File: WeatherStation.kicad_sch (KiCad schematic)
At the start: 9 parts

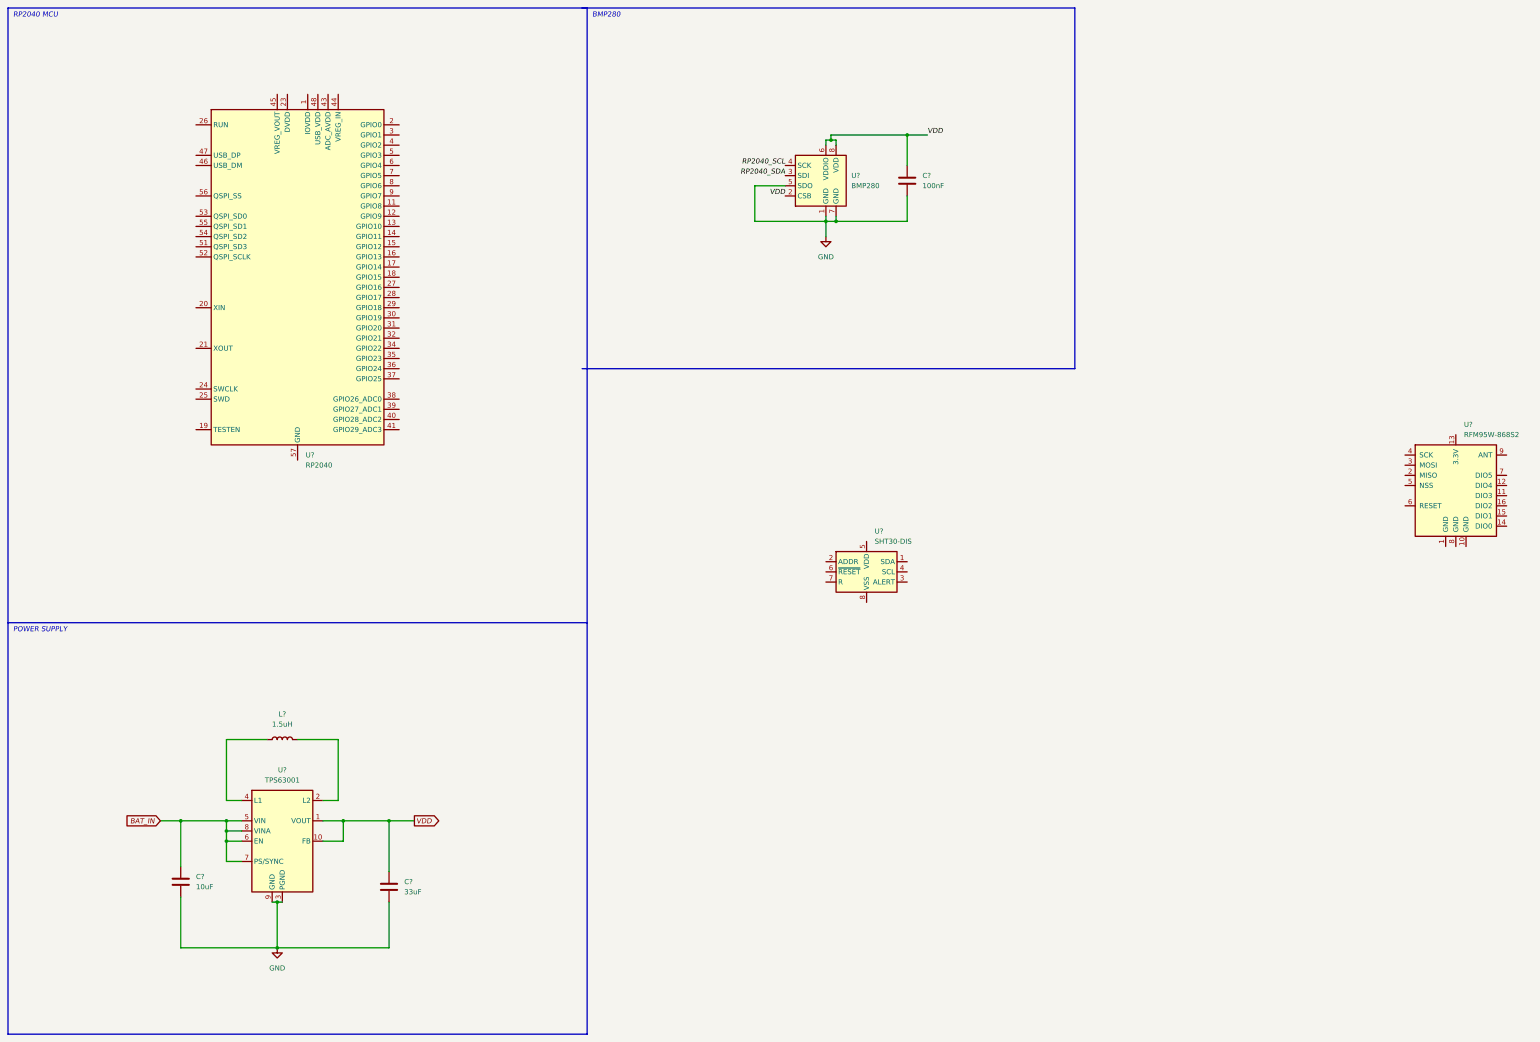
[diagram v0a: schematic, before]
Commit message: some capatitiors and sensors
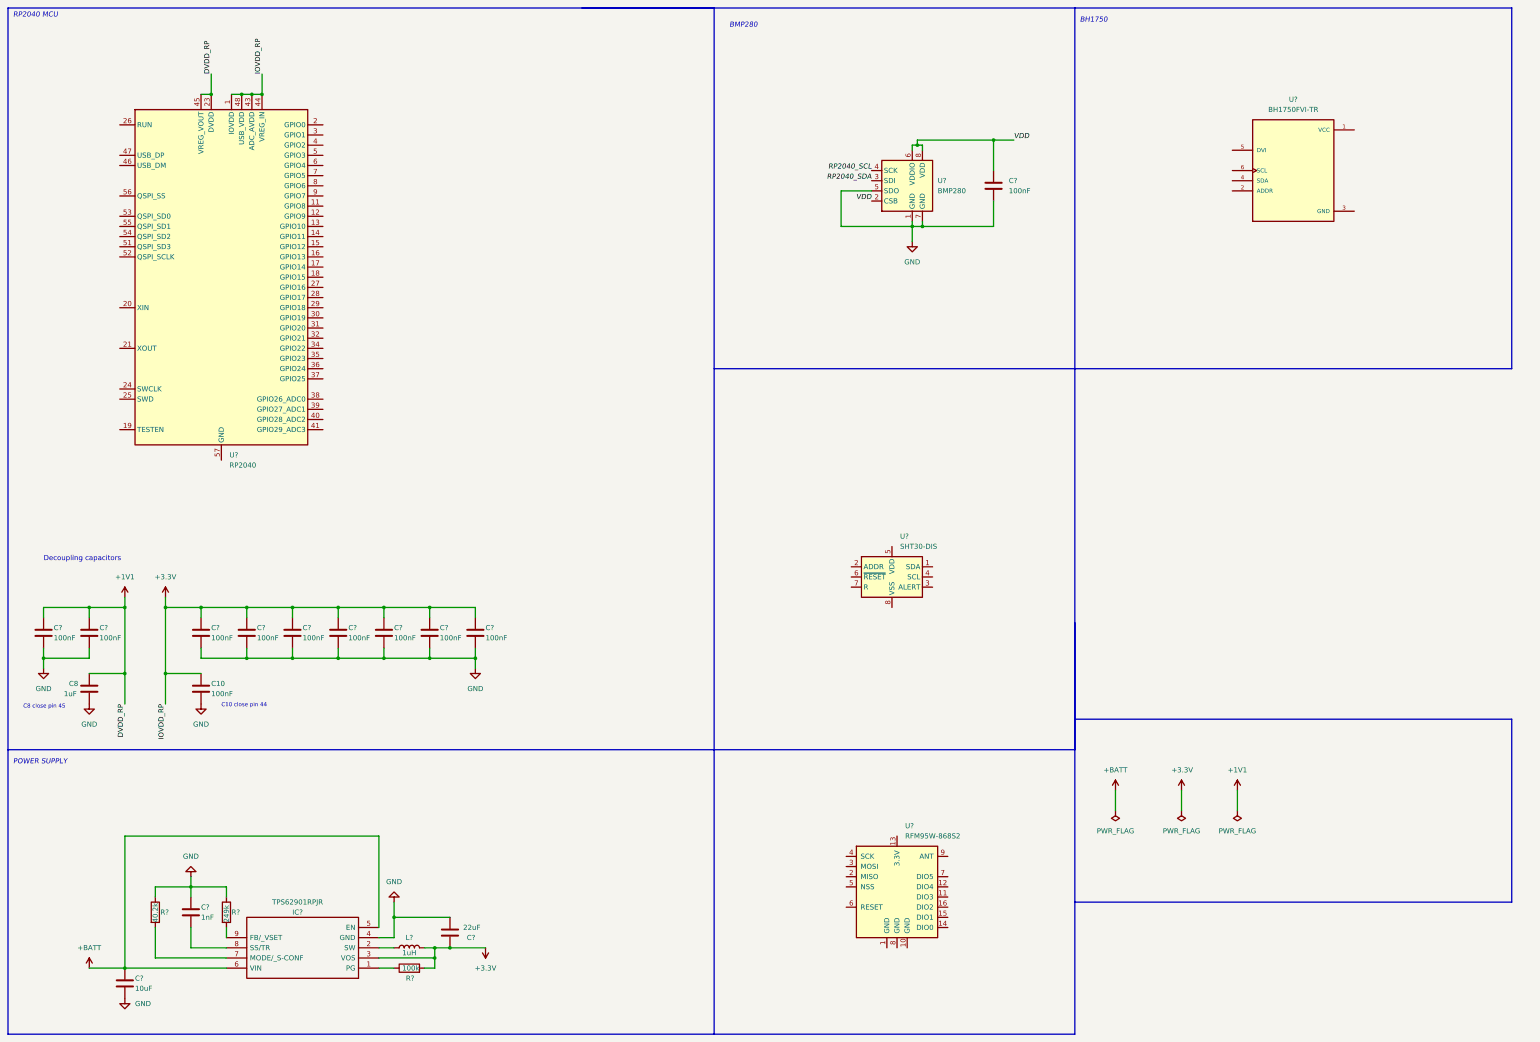
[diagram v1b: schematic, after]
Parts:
- removed C?: 33uF, symbol Device:C
- removed C?: 10uF, symbol Device:C
- removed L?: 1.5uH, symbol Device:L
- removed U?: TPS63001, Package_SON:Texas_DRC0010J_ThermalVias, symbol Regulator_Switching:TPS63001
- added C10, C? (x9): 100nF, symbol Device:C
- added C8: 1uF, symbol Device:C
- added C?: 22uF, symbol Device:C
- added C?: 1nF, symbol Device:C
- added C?: 10uF, symbol Device:C
- added IC?: TPS62901RPJR, TPS62901RPJR, symbol TPS62901RPJR:TPS62901RPJR
- added L?: 1uH, symbol Device:L
- added R?: 40.2k, symbol Device:R
- added R?: 249k, symbol Device:R
- added R?: 100k, symbol Device:R
- added U?: BH1750FVI-TR, XDCR_BH1750FVI-TR, symbol BH1750:BH1750FVI-TR
- U?: footprint (none) -> RF_Module:HOPERF_RFM9XW_SMD
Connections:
- net GND: now also C10.2, C8.2, C?.1, C?.2, C?.2, C?.2, C?.2, C?.2, C?.2, C?.2, C?.2, C?.2, C?.2, C?.2, IC?.4 (GND), R?.1, R?.1
- net +3.3V: now reaches U?.1 (IOVDD), U?.10 (IOVDD), U?.22 (IOVDD), U?.33 (IOVDD), U?.42 (IOVDD), U?.49 (IOVDD)
- net +3.3V: now also U?.43 (ADC_AVDD), U?.44 (VREG_IN), U?.48 (USB_VDD), C10.1, C?.1, C?.1, C?.1, C?.1, C?.1, C?.1, C?.1, C?.1, IC?.3 (VOS), L?.2, R?.2
- net +1V1: now reaches U?.23 (DVDD), U?.50 (DVDD)
- net +1V1: now also U?.45 (VREG_VOUT), C8.1, C?.1, C?.1
- new net: IC?.7 (MODE/_S-CONF), R?.2
- new net: IC?.1 (PG), R?.1
- new net: IC?.2 (SW), L?.1
- new net: C?.2, IC?.8 (SS/TR)
- new net: IC?.9 (FB/_VSET), R?.2
- new net +BATT: C?.1, IC?.5 (EN), IC?.6 (VIN)
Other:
- note added: "BH1750"
- note added: "C10 close pin 44"
- note added: "C8 close pin 45"
- note added: "Decoupling capacitors"
- moved on the sheet: C?, U?

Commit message: kabelki
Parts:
- added AE?: Antenna, symbol Device:Antenna
- added C? (x2): 27pF, symbol Device:C
- added C?: 0.1uF, symbol Device:C
- added C? (x2): 100nF, symbol Device:C
- added C?: 10uF, symbol Device:C_Polarized
- added J? (x2): Conn_01x02, symbol Connector_Generic:Conn_01x02
- added R? (x4): 1k, symbol Device:R
- added R? (x4): 10k, symbol Device:R
- added R? (x2): 27, symbol Device:R
- added R?: DNF, symbol Device:R
- added U?: W25Q128JVSIQ, SOIC127P790X216-8N, symbol Flashs:W25Q128JVSIQ
- added Y?: Crystal, symbol Device:Crystal
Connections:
- net VDD is gone; now on net +3.3V: C?.1, U?.2 (CSB), U?.6 (VDDIO), U?.8 (VDD)
- net +3.3V: now also U?.1 (VCC), U?.5 (VDD), C?.1, C?.1, C?.2, R?.1, R?.1, R?.1, R?.2, R?.2, R?.2, U?.8 (VCC)
- net GND: now also U?.1 (GND), U?.10 (GND), U?.2 (ADDR), U?.3 (GND), U?.57 (GND), U?.6 (RESET), U?.6 (~{RESET}), U?.7 (R), U?.8 (GND), U?.8 (VSS), U?.9 (VSS), C?.1, C?.1, C?.1, C?.2, C?.2, C?.2, J?.2 (Pin_2), R?.1, U?.4 (GND)
- net at U?.2 (ADDR): now also R?.2
- net SDA: now reaches U?.4 (SDA)
- net SDA: now also U?.1 (SDA), R?.1, R?.2
- net at U?.5 (DVI): now also C?.1, R?.1
- net SCL: now reaches U?.6 (SCL)
- net SCL: now also U?.4 (SCL), R?.1, R?.2
- net GPIO_ALERT_SHT30: now reaches U?.3 (ALERT)
- net GPIO_ALERT_SHT30: now also U?.2 (GPIO0)
- net DIO2_LORA: now reaches U?.11 (DIO3)
- net DIO1_LORA: now reaches U?.12 (DIO4)
- net DIO5_LORA: now reaches U?.14 (DIO0)
- net DIO4_LORA: now reaches U?.15 (DIO1)
- net DIO3_LORA: now reaches U?.16 (DIO2)
- net MISO_LORA: now reaches U?.2 (MISO)
- net MOSI_LORA: now reaches U?.3 (MOSI)
- net SCK_LORA: now reaches U?.4 (SCK)
- net CS_LORA: now reaches U?.5 (NSS)
- net DIO0_LORA: now reaches U?.7 (DIO5)
- net at U?.9 (ANT): now also AE?.1 (A)
- net TESTEN: now reaches U?.19 (TESTEN)
- net XIN: now reaches U?.20 (XIN)
- net XIN: now also C?.2, Y?.2
- net XOUT: now reaches U?.21 (XOUT)
- net XOUT: now also R?.2
- net SWCLK: now reaches U?.24 (SWCLK)
- net SWD: now reaches U?.25 (SWD)
- net RUN: now reaches U?.26 (RUN)
- net at U?.46 (USB_DM): now also R?.1
- net at U?.47 (USB_DP): now also R?.1
- net QSPI_SD3: now reaches U?.51 (QSPI_SD3)
- net QSPI_SD3: now also U?.7 (/HOLD/RESET(IO3))
- net QSPI_SCLK: now reaches U?.52 (QSPI_SCLK)
- net QSPI_SCLK: now also U?.6 (CLK)
- net QSPI_SD0: now reaches U?.53 (QSPI_SD0)
- net QSPI_SD0: now also U?.5 (DI(IO0))
- net QSPI_SD2: now reaches U?.54 (QSPI_SD2)
- net QSPI_SD2: now also U?.3 (/WP(IO2))
- net QSPI_SD1: now reaches U?.55 (QSPI_SD1)
- net QSPI_SD1: now also U?.2 (DO(IO1))
- net QSPI_SS: now reaches U?.56 (QSPI_SS)
- net QSPI_SS: now also R?.2, R?.2, U?.1 (/CS)
- new net: C?.2, R?.1, Y?.1
- new net USB_BOOT: J?.1 (Pin_1), R?.1
- new net USB_D+: J?.1 (Pin_1), R?.2
- new net USB_D-: J?.2 (Pin_2), R?.2
- no-connect marks 0 -> 4
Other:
- note added: "Flash"
- note added: "Oscilator"
- note added: "R3, R4 close RP2040"
- note added: "STH30"
- moved on the sheet: C?, U?

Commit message: PCB lets gooo
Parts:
- added SW1: SW_Push, Button_Switch_SMD:SW_Push_1P1T_NO_CK_KSC6xxJ, symbol Switch:SW_Push
- AE1: renamed from AE?; footprint (none) -> Connector_Coaxial:SMA_Amphenol_901-144_Vertical
- C1, C11, C12, C13, C14, C15, C16, C17, C18, C19, C2, C20, C3, C4, C5, C6, C7, C9: renamed from C?; footprint (none) -> Capacitor_SMD:C_0603_1608Metric_Pad1.08x0.95mm_HandSolder
- C10, C8: footprint (none) -> Capacitor_SMD:C_0603_1608Metric_Pad1.08x0.95mm_HandSolder
- C21: renamed from C?; value 0.1uF -> 100nF; footprint (none) -> Capacitor_SMD:C_0603_1608Metric_Pad1.08x0.95mm_HandSolder
- IC1: renamed from IC?; footprint TPS62901RPJR -> TPS62901RPJR:TPS62901RPJR
- J1, J2: renamed from J?; footprint (none) -> Connector_PinHeader_2.54mm:PinHeader_1x02_P2.54mm_Vertical
- L1: renamed from L?; footprint (none) -> Inductor_SMD:L_0603_1608Metric_Pad1.05x0.95mm_HandSolder
- R1, R10, R11, R12, R13, R14, R2, R3, R4, R5, R6, R7, R8, R9: renamed from R?; footprint (none) -> Resistor_SMD:R_0603_1608Metric_Pad0.98x0.95mm_HandSolder
- U2: renamed from U?; footprint SOIC127P790X216-8N -> Flashs:SOIC127P790X216-8N
- U6: renamed from U?; footprint XDCR_BH1750FVI-TR -> BH1750:XDCR_BH1750FVI-TR
- Y1: renamed from Y?; footprint (none) -> Crystal:Crystal_SMD_HC49-SD_HandSoldering
- gave numbers to parts that had none: 4
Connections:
- net RP2040_SCL is gone; now on net SCL: U5.4 (SCK)
- net RP2040_SDA is gone; now on net SDA: U5.3 (SDI)
- net +3.3V: now also U3.13 (3.3V)
- net CS_LORA: now also U1.7 (GPIO5)
- net DIO0_LORA: now also U1.12 (GPIO9)
- net DIO1_LORA: now also U1.13 (GPIO10)
- net DIO2_LORA: now also U1.14 (GPIO11)
- net DIO3_LORA: now also U1.15 (GPIO12)
- net DIO4_LORA: now also U1.16 (GPIO13)
- net DIO5_LORA: now also U1.17 (GPIO14)
- net GND: now also SW1.1
- net GPIO_ALERT_SHT30: now also U1.11 (GPIO8); no longer U1.2 (GPIO0)
- net MISO_LORA: now also U1.9 (GPIO7)
- net MOSI_LORA: now also U1.6 (GPIO4)
- net SCK_LORA: now also U1.8 (GPIO6)
- net SCL: now also U1.3 (GPIO1)
- net SDA: now also U1.2 (GPIO0)
- net RUN: no longer names the net of U1.26 (RUN)
- net RUN: now also SW1.2
- net SWCLK: no longer names the net of U1.24 (SWCLK)
- net SWD: no longer names the net of U1.25 (SWD)
- net TESTEN: no longer names the net of U1.19 (TESTEN)
- no-connect marks 4 -> 20

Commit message: Some puzzle
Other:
- note added: "R1, R2 close RP2040"
- note removed: "R3, R4 close RP2040"
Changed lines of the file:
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@@
     (effects (font (size 1.27 1.27)) (justify right bottom))
   )
-  (text "R3, R4 close RP2040\n" (at 27.94 49.53 0)
+  (text "R1, R2 close RP2040\n" (at 27.94 49.53 0)
     (effects (font (size 1 1)) (justify left bottom))
   )

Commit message: PCB layout update
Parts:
- added J3: Conn_01x02, Connector_PinHeader_2.54mm:PinHeader_1x02_P2.54mm_Vertical, symbol Connector_Generic:Conn_01x02
- SW1: footprint Button_Switch_SMD:SW_Push_1P1T_NO_CK_KSC6xxJ -> Button_Switch_SMD:SW_SPST_TL3305A
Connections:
- net +BATT: now also J3.1 (Pin_1)
- net GND: now also J3.2 (Pin_2)
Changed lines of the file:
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@@
   (junction (at 73.66 38.1) (diameter 0) (color 0 0 0 0)
+  )
+  (junction (at 39.37 260.35) (diameter 0) (color 0 0 0 0)
   )
   (junction (at 308.61 72.39) (diameter 0) (color 0 0 0 0)
@@
     (stroke (width 0) (type default) (color 0 0 0 0))
   )
-  (wire (pts (xy 43.18 260.35) (xy 52.07 260.35))
+  (wire (pts (xy 30.48 260.35) (xy 39.37 260.35))
     (stroke (width 0) (type default) (color 0 0 0 0))
   )
@@
     (stroke (width 0) (type default) (color 0 0 0 0))
   )
+  (wire (pts (xy 39.37 260.35) (xy 52.07 260.35))
+    (stroke (width 0) (type default) (color 0 0 0 0))
+  )
   (wire (pts (xy 182.88 88.9) (xy 185.42 88.9))
     (stroke (width 0) (type default) (color 0 0 0 0))
@@
   )
   (polyline (pts (xy 398.78 205.74) (xy 289.56 205.74))
+    (stroke (width 0) (type default) (color 0 0 0 0))
+  )
+  (wire (pts (xy 39.37 233.68) (xy 39.37 260.35))
     (stroke (width 0) (type default) (color 0 0 0 0))
   )
@@
     )
     (property "Datasheet" "" (id 3) (at 68.58 237.49 0)
+      (effects (font (size 1.27 1.27)) hide)
+    )
+    (pin "1")
+  )
+  (symbol (lib_id "power:GND") (at 41.91 233.68 0) (unit 1)
+    (in_bom yes) (on_board yes) (fields_autoplaced)
+    (property "Reference" "#PWR0116" (id 0) (at 41.91 240.03 0)
+      (effects (font (size 1.27 1.27)) hide)
+    )
+    (property "Value" "GND" (id 1) (at 44.45 234.9499 0)
+      (effects (font (size 1.27 1.27)) (justify left))
+    )
+    (property "Footprint" "" (id 2) (at 41.91 233.68 0)
+      (effects (font (size 1.27 1.27)) hide)
+    )
+    (property "Datasheet" "" (id 3) (at 41.91 233.68 0)
       (effects (font (size 1.27 1.27)) hide)
     )
@@
     (pin "1")
   )
-  (symbol (lib_id "power:+BATT") (at 43.18 260.35 0) (unit 1)
+  (symbol (lib_id "power:+BATT") (at 30.48 260.35 0) (unit 1)
     (in_bom yes) (on_board yes) (fields_autoplaced)
-    (property "Reference" "#PWR0109" (id 0) (at 43.18 264.16 0)
-      (effects (font (size 1.27 1.27)) hide)
-    )
-    (property "Value" "+BATT" (id 1) (at 43.18 255.27 0))
-    (property "Footprint" "" (id 2) (at 43.18 260.35 0)
-      (effects (font (size 1.27 1.27)) hide)
-    )
-    (property "Datasheet" "" (id 3) (at 43.18 260.35 0)
+    (property "Reference" "#PWR0109" (id 0) (at 30.48 264.16 0)
+      (effects (font (size 1.27 1.27)) hide)
+    )
+    (property "Value" "+BATT" (id 1) (at 30.48 255.27 0))
+    (property "Footprint" "" (id 2) (at 30.48 260.35 0)
+      (effects (font (size 1.27 1.27)) hide)
+    )
+    (property "Datasheet" "" (id 3) (at 30.48 260.35 0)
       (effects (font (size 1.27 1.27)) hide)
     )
@@
     (property "Reference" "SW1" (id 0) (at 36.83 27.94 0))
     (property "Value" "SW_Push" (id 1) (at 36.83 30.48 0))
-    (property "Footprint" "Button_Switch_SMD:SW_Push_1P1T_NO_CK_KSC6xxJ" (id 2) (at 36.83 30.48 0)
-      (effects (font (size 1.27 1.27)) hide)
-    )
+    (property "Footprint" "Button_Switch_SMD:SW_SPST_TL3305A" (id 2) (at 36.83 30.48 0))
     (property "Datasheet" "~" (id 3) (at 36.83 30.48 0)
       (effects (font (size 1.27 1.27)) hide)
@@
     )
     (property "Datasheet" "~" (id 3) (at 265.43 63.5 0)
+      (effects (font (size 1.27 1.27)) hide)
+    )
+    (pin "1")
+    (pin "2")
+  )
+  (symbol (lib_id "Connector_Generic:Conn_01x02") (at 39.37 228.6 90) (unit 1)
+    (in_bom yes) (on_board yes)
+    (property "Reference" "J3" (id 0) (at 46.99 228.6 90)
+      (effects (font (size 1.27 1.27)) (justify left))
+    )
+    (property "Value" "Conn_01x02" (id 1) (at 35.56 228.6 90)
+      (effects (font (size 1.27 1.27)) (justify left) hide)
+    )
+    (property "Footprint" "Connector_PinHeader_2.54mm:PinHeader_1x02_P2.54mm_Vertical" (id 2) (at 39.37 228.6 0)
+      (effects (font (size 1.27 1.27)) hide)
+    )
+    (property "Datasheet" "~" (id 3) (at 39.37 228.6 0)
       (effects (font (size 1.27 1.27)) hide)
     )
@@
       (reference "#PWR0115") (unit 1) (value "+3.3V") (footprint "")
     )
+    (path "/195bd33f-2193-4828-beaa-1b37f00c6c31"
+      (reference "#PWR0116") (unit 1) (value "GND") (footprint "")
+    )
     (path "/5eb9dfef-1e2b-447f-99c5-7efaa10ff2d8"
       (reference "AE1") (unit 1) (value "Antenna") (footprint "Connector_Coaxial:SMA_Amphenol_901-144_Vertical")
@@
       (reference "J2") (unit 1) (value "Conn_01x02") (footprint "Connector_PinHeader_2.54mm:PinHeader_1x02_P2.54mm_Vertical")
     )
+    (path "/e9a2a3ea-06b6-4923-a2a1-584823b95ae6"
+      (reference "J3") (unit 1) (value "Conn_01x02") (footprint "Connector_PinHeader_2.54mm:PinHeader_1x02_P2.54mm_Vertical")
+    )
     (path "/de0add37-8b08-471a-b0cc-dec6edd73a8f"
       (reference "L1") (unit 1) (value "1uH") (footprint "Inductor_SMD:L_0603_1608Metric_Pad1.05x0.95mm_HandSolder")
@@
     )
     (path "/c11470c5-4829-48b1-98a7-568462c64a84"
-      (reference "SW1") (unit 1) (value "SW_Push") (footprint "Button_Switch_SMD:SW_Push_1P1T_NO_CK_KSC6xxJ")
+      (reference "SW1") (unit 1) (value "SW_Push") (footprint "Button_Switch_SMD:SW_SPST_TL3305A")
     )
     (path "/fa393eb2-1c54-4621-8b5b-b7b031a8a7c9"
